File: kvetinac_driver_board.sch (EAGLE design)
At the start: 149 parts, among them IC1 MEGA128-A, IC3 74HC238D, IC4 VNH2SP30, IC5 VNH2SP30, J1 PINHD-1X1SMD2.4MM, J10 PINHD-1X1SMD2.4MM, J11 PINHD-1X1SMD2.4MM, J12 PINHD-1X1SMD2.4MM, J13 PINHD-1X1SMD2.4MM, J14 PINHD-1X1SMD2.4MM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

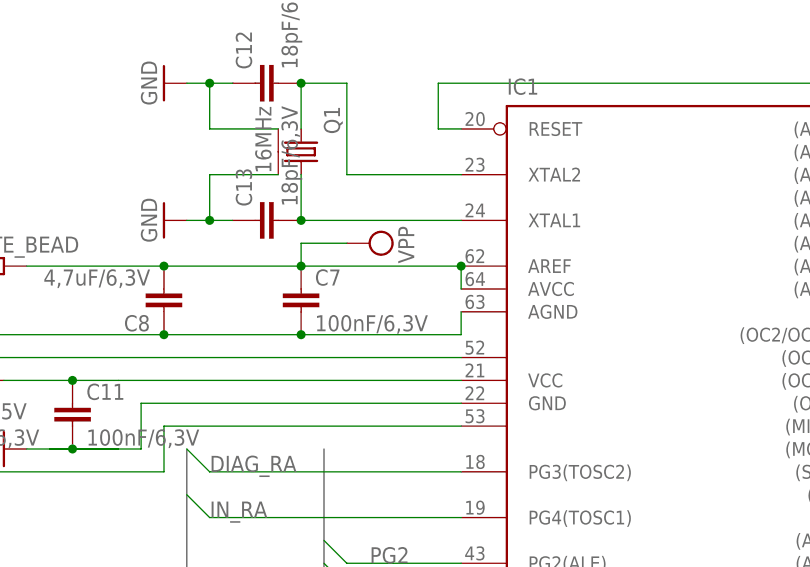
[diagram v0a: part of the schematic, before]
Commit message: AREF pripojen pres 100nF ke GND, misto k AVCC - umoznuje pouzit interni 2.56V referenci
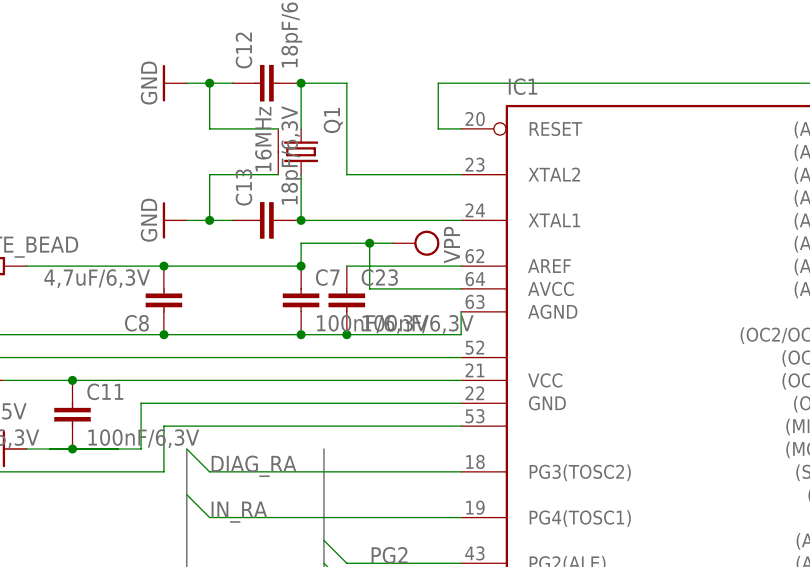
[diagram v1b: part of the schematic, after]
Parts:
- added C23: 100nF/6,3V, rcl_upravena:C-EUC0306
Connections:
- new net AREF: C23.1, IC1.AREF
- net GND: now also C23.2
- net VPP: no longer IC1.AREF
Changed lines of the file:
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@@
 <part name="Q3" library="vacha" deviceset="TPCA8128" device="SO8"/>
 <part name="GND5" library="supply1" deviceset="GND" device=""/>
+<part name="C23" library="rcl_upravena" deviceset="C-EU" device="C0306" value="100nF/6,3V"/>
 </parts>
 <sheets>
@@
 <instance part="GND30" gate="1" x="111.76" y="12.7" rot="R270"/>
 <instance part="GND_ADC1" gate="A" x="220.98" y="76.2" rot="R180"/>
-<instance part="SUPPLY1" gate="G$1" x="60.96" y="-73.66" rot="R270"/>
+<instance part="SUPPLY1" gate="G$1" x="66.04" y="-73.66" rot="R270"/>
 <instance part="SUPPLY2" gate="G$1" x="231.14" y="91.44"/>
 <instance part="ADC" gate="A" x="205.74" y="76.2"/>
@@
 <instance part="Q3" gate="G$1" x="109.22" y="91.44" rot="R180"/>
 <instance part="GND5" gate="1" x="93.98" y="83.82"/>
+<instance part="C23" gate="G$1" x="58.42" y="-78.74"/>
 </instances>
 <busses>
@@
 <segment>
 <wire x1="71.12" y1="-81.28" x2="71.12" y2="-83.82" width="0.1524" layer="91"/>
-<wire x1="53.34" y1="-83.82" x2="71.12" y2="-83.82" width="0.1524" layer="91"/>
+<wire x1="53.34" y1="-83.82" x2="58.42" y2="-83.82" width="0.1524" layer="91"/>
+<wire x1="58.42" y1="-83.82" x2="71.12" y2="-83.82" width="0.1524" layer="91"/>
 <wire x1="53.34" y1="-83.82" x2="38.1" y2="-83.82" width="0.1524" layer="91"/>
 <wire x1="38.1" y1="-83.82" x2="15.24" y2="-83.82" width="0.1524" layer="91"/>
@@
 <pinref part="C7" gate="G$1" pin="2"/>
 <pinref part="C8" gate="G$1" pin="1"/>
+<pinref part="C23" gate="G$1" pin="2"/>
+<junction x="58.42" y="-83.82"/>
 </segment>
 <segment>
@@
 <net name="VPP" class="0">
 <segment>
-<wire x1="71.12" y1="-76.2" x2="53.34" y2="-76.2" width="0.1524" layer="91"/>
 <wire x1="53.34" y1="-76.2" x2="38.1" y2="-76.2" width="0.1524" layer="91"/>
 <wire x1="38.1" y1="-76.2" x2="22.86" y2="-76.2" width="0.1524" layer="91"/>
-<wire x1="71.12" y1="-78.74" x2="71.12" y2="-76.2" width="0.1524" layer="91"/>
-<wire x1="58.42" y1="-73.66" x2="53.34" y2="-73.66" width="0.1524" layer="91"/>
+<wire x1="63.5" y1="-73.66" x2="60.96" y2="-73.66" width="0.1524" layer="91"/>
+<wire x1="60.96" y1="-73.66" x2="53.34" y2="-73.66" width="0.1524" layer="91"/>
 <wire x1="53.34" y1="-73.66" x2="53.34" y2="-76.2" width="0.1524" layer="91"/>
-<junction x="71.12" y="-76.2"/>
 <junction x="53.34" y="-76.2"/>
 <junction x="38.1" y="-76.2"/>
-<pinref part="IC1" gate="G$1" pin="AREF"/>
-<pinref part="IC1" gate="G$1" pin="AVCC"/>
 <pinref part="FERITE_BEAD" gate="G$1" pin="2"/>
 <pinref part="C7" gate="G$1" pin="1"/>
 <pinref part="SUPPLY1" gate="G$1" pin="VPP"/>
 <pinref part="C8" gate="G$1" pin="2"/>
+<pinref part="IC1" gate="G$1" pin="AVCC"/>
+<wire x1="71.12" y1="-78.74" x2="60.96" y2="-78.74" width="0.1524" layer="91"/>
+<wire x1="60.96" y1="-78.74" x2="60.96" y2="-73.66" width="0.1524" layer="91"/>
+<junction x="60.96" y="-73.66"/>
 </segment>
 <segment>
@@
 </segment>
 </net>
+<net name="AREF" class="0">
+<segment>
+<pinref part="IC1" gate="G$1" pin="AREF"/>
+<pinref part="C23" gate="G$1" pin="1"/>
+<wire x1="71.12" y1="-76.2" x2="58.42" y2="-76.2" width="0.1524" layer="91"/>
+</segment>
+</net>

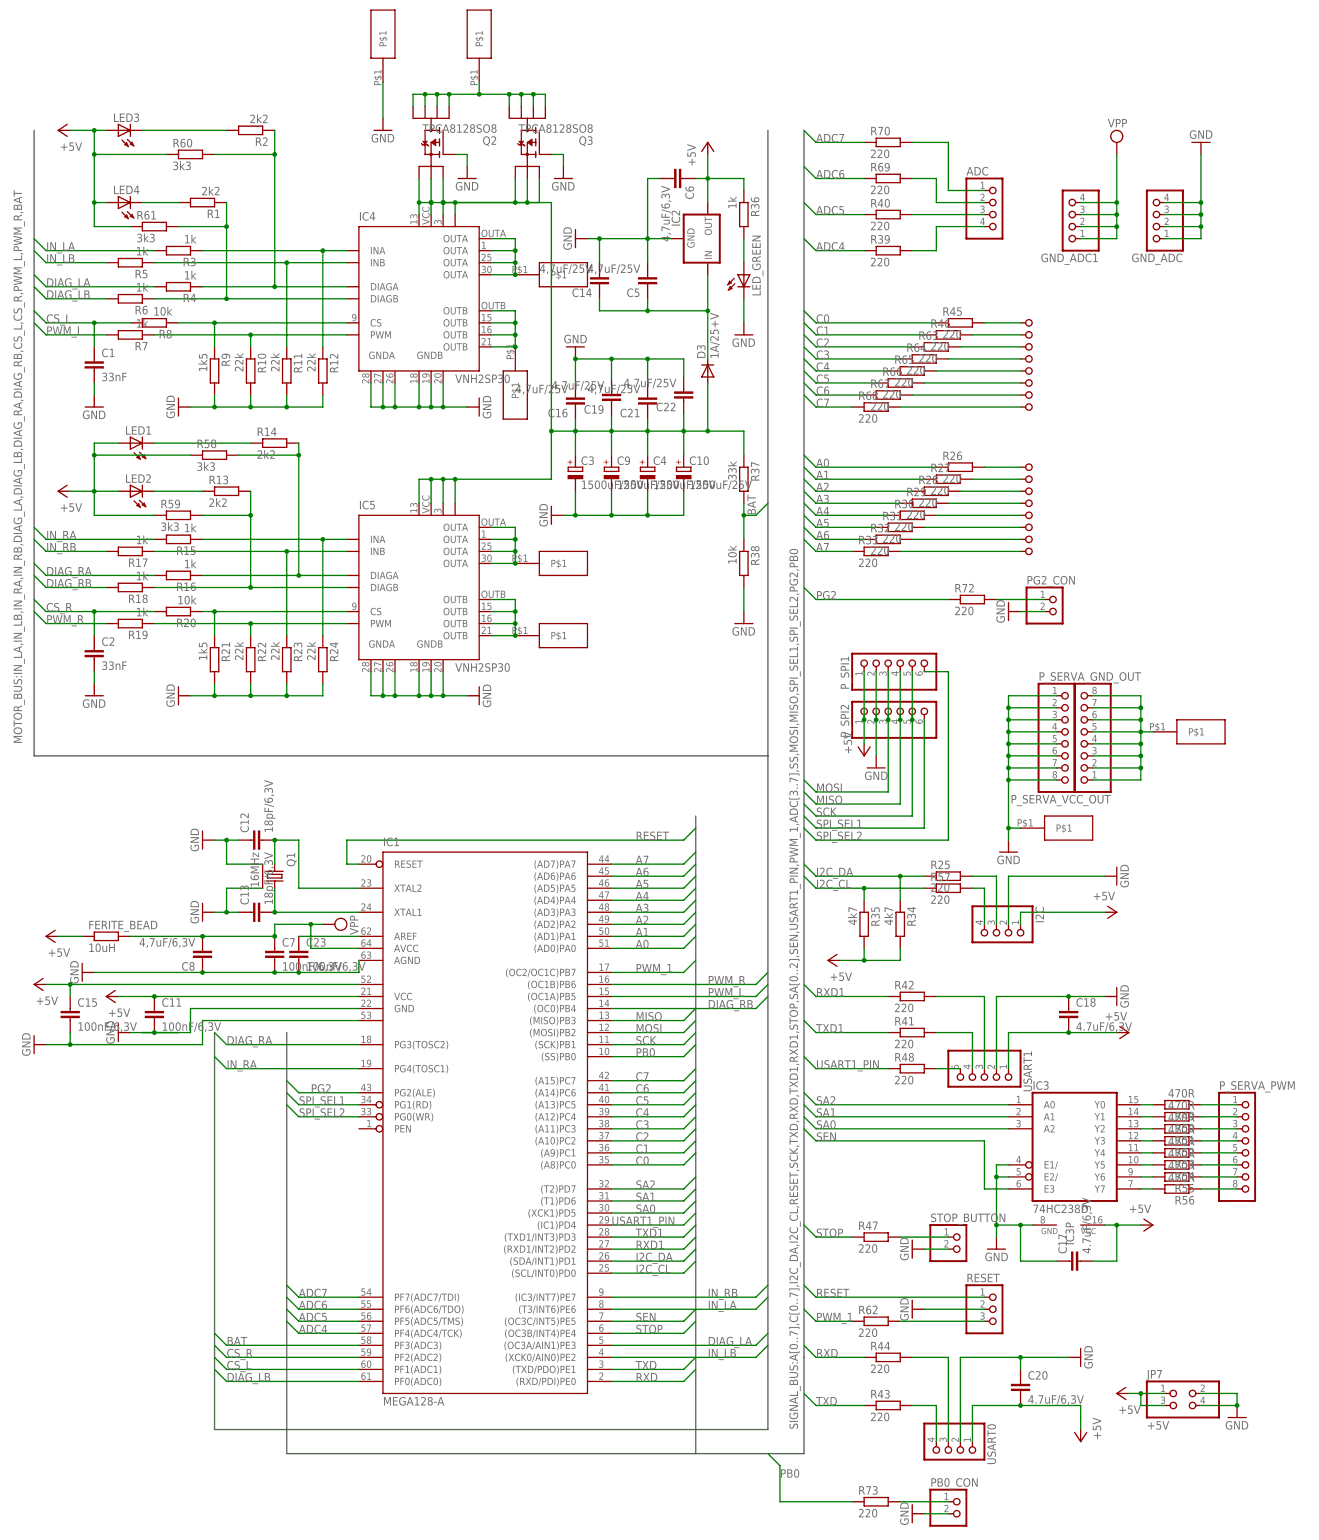
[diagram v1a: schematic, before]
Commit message: Upraven popis soucastek (Led1 az Led4 a kondenzatory C17, C18, C20).
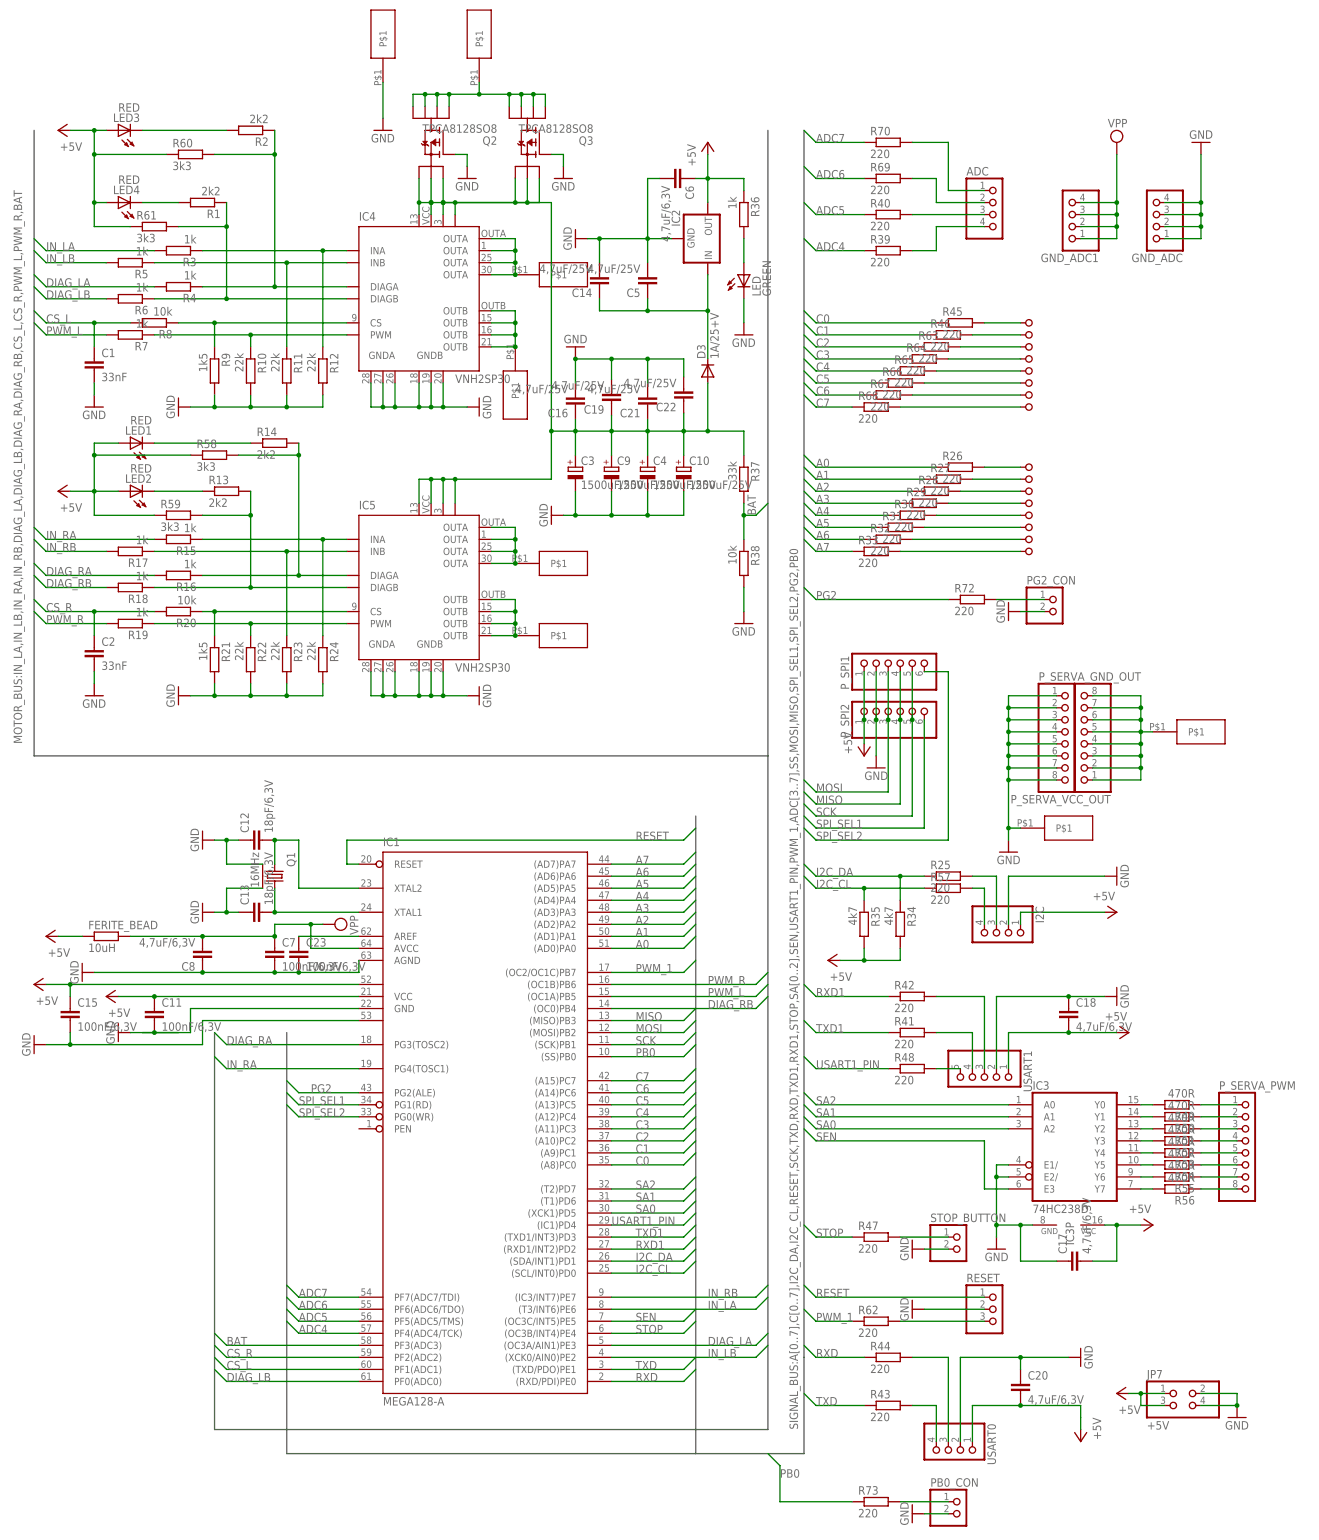
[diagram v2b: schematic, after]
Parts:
- C17, C18, C20: value 4.7uF/6,3V -> 4,7uF/6,3V
- LED: value (none) -> GREEN
- LED1, LED2, LED3, LED4: value (none) -> RED
- renumbered LED_GREEN to LED
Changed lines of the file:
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@@
 <?xml version="1.0" encoding="utf-8"?>
 <!DOCTYPE eagle SYSTEM "eagle.dtd">
-<eagle version="6.2">
+<eagle version="6.1">
 <drawing>
 <settings>
@@
 <part name="R34" library="rcl" deviceset="R-EU_" device="R0603" value="4k7"/>
 <part name="R35" library="rcl" deviceset="R-EU_" device="R0603" value="4k7"/>
-<part name="LED_GREEN" library="led" deviceset="LED" device="CHIPLED_0805"/>
+<part name="LED" library="led" deviceset="LED" device="CHIPLED_0805" value="GREEN"/>
 <part name="R36" library="rcl" deviceset="R-EU_" device="R0603" value="1k"/>
 <part name="FERITE_BEAD" library="rcl" deviceset="R-EU_" device="R0603" value="10uH"/>
@@
 <part name="R47" library="rcl" deviceset="R-EU_" device="R0603" value="220"/>
 <part name="GND17" library="supply1" deviceset="GND" device=""/>
-<part name="LED1" library="led" deviceset="LED" device="CHIPLED_0805"/>
-<part name="LED2" library="led" deviceset="LED" device="CHIPLED_0805"/>
-<part name="LED3" library="led" deviceset="LED" device="CHIPLED_0805"/>
-<part name="LED4" library="led" deviceset="LED" device="CHIPLED_0805"/>
+<part name="LED1" library="led" deviceset="LED" device="CHIPLED_0805" value="RED"/>
+<part name="LED2" library="led" deviceset="LED" device="CHIPLED_0805" value="RED"/>
+<part name="LED3" library="led" deviceset="LED" device="CHIPLED_0805" value="RED"/>
+<part name="LED4" library="led" deviceset="LED" device="CHIPLED_0805" value="RED"/>
 <part name="IC3" library="74" deviceset="74*238" device="D" technology="HC"/>
 <part name="R49" library="rcl" deviceset="R-EU_" device="R0603" value="470R"/>
@@
 <part name="R70" library="rcl" deviceset="R-EU_" device="R0603" value="220"/>
 <part name="GND27" library="supply1" deviceset="GND" device=""/>
-<part name="C17" library="rcl" deviceset="C-EU" device="C0805" value="4.7uF/6,3V"/>
-<part name="C18" library="rcl" deviceset="C-EU" device="C0805" value="4.7uF/6,3V"/>
-<part name="C20" library="rcl" deviceset="C-EU" device="C0805" value="4.7uF/6,3V"/>
+<part name="C17" library="rcl" deviceset="C-EU" device="C0805" value="4,7uF/6,3V"/>
+<part name="C18" library="rcl" deviceset="C-EU" device="C0805" value="4,7uF/6,3V"/>
+<part name="C20" library="rcl" deviceset="C-EU" device="C0805" value="4,7uF/6,3V"/>
 <part name="IC4" library="vacha" deviceset="VNH2SP30" device=""/>
 <part name="IC5" library="vacha" deviceset="VNH2SP30" device=""/>
@@
 <instance part="R34" gate="G$1" x="185.42" y="-73.66" rot="R270"/>
 <instance part="R35" gate="G$1" x="177.8" y="-73.66" rot="R270"/>
-<instance part="LED_GREEN" gate="G$1" x="152.4" y="63.5"/>
+<instance part="LED" gate="G$1" x="152.4" y="63.5"/>
 <instance part="R36" gate="G$1" x="152.4" y="76.2" rot="R270"/>
 <instance part="FERITE_BEAD" gate="G$1" x="17.78" y="-76.2"/>
@@
 <wire x1="152.4" y1="53.34" x2="152.4" y2="58.42" width="0.1524" layer="91"/>
 <pinref part="GND7" gate="1" pin="GND"/>
-<pinref part="LED_GREEN" gate="G$1" pin="C"/>
+<pinref part="LED" gate="G$1" pin="C"/>
 </segment>
 <segment>
@@
 <wire x1="152.4" y1="71.12" x2="152.4" y2="66.04" width="0.1524" layer="91"/>
 <pinref part="R36" gate="G$1" pin="2"/>
-<pinref part="LED_GREEN" gate="G$1" pin="A"/>
-</segment>
-</net>
+<pinref part="LED" gate="G$1" pin="A"/>
+</segment>
+</net>
